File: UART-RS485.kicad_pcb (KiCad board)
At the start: 2 copper layers, 16.5 x 40 mm, 4 parts, among them J1 Conn_01x04, J2 Conn_01x05, U1 SP3485EN

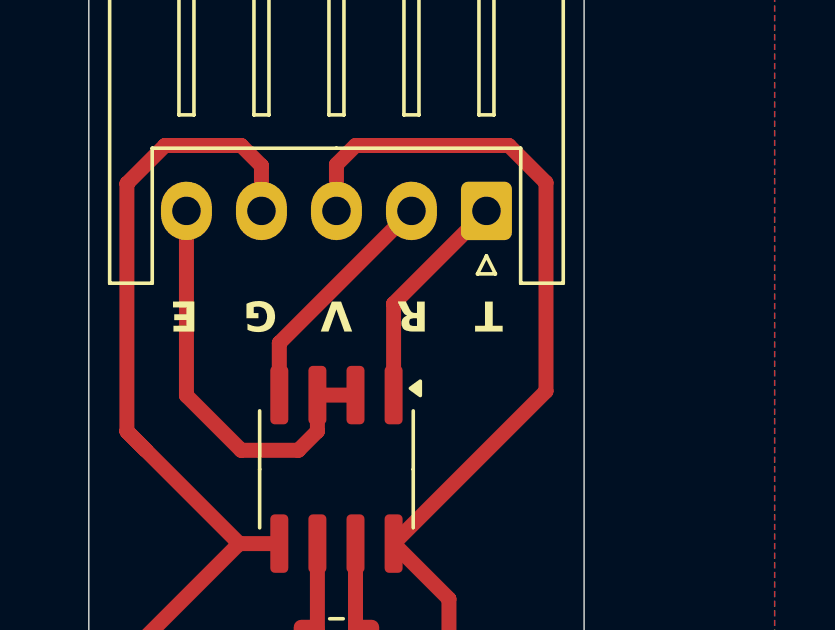
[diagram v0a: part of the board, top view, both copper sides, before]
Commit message: add tx rx arrow
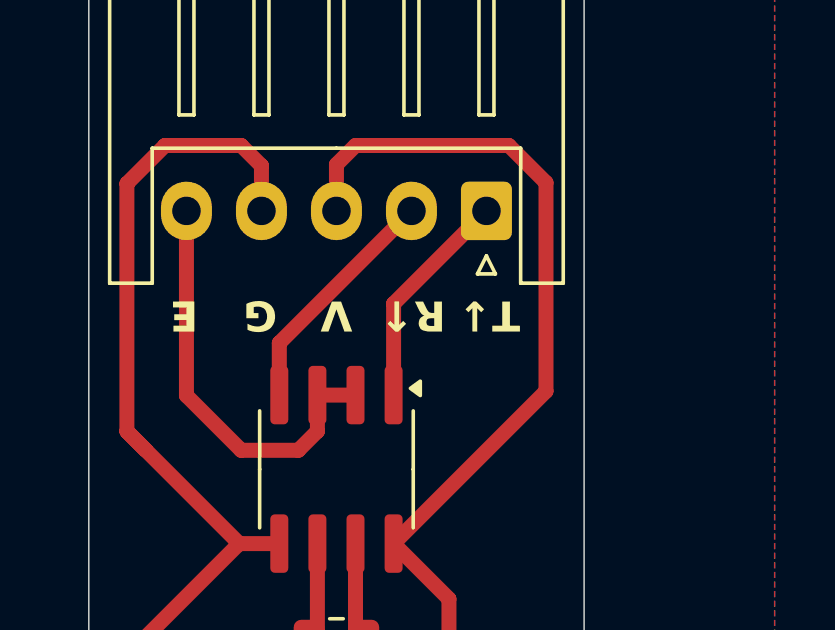
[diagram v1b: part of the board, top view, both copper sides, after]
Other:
- board text added: "R↑"
- board text added: "T↓"
- board text removed: "R"
- board text removed: "T"
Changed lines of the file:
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@@
 		(layer "Edge.Cuts")
 	)
-	(gr_text "T"
+	(gr_text "T↓"
 		(at 140.335 99.695 180)
 		(layer "F.SilkS")
@@
 		)
 	)
-	(gr_text "R"
+	(gr_text "R↑"
 		(at 137.795 99.695 180)
 		(layer "F.SilkS")
